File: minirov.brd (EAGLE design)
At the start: 65.8 x 30.7 mm, 55 parts, among them Q1 DMN6140L-13DICT-ND, Q2 DMN6140L-13DICT-ND, U1 DRV8848PWP, U2 DRV8848PWP, U3 MAX1136EUA-T

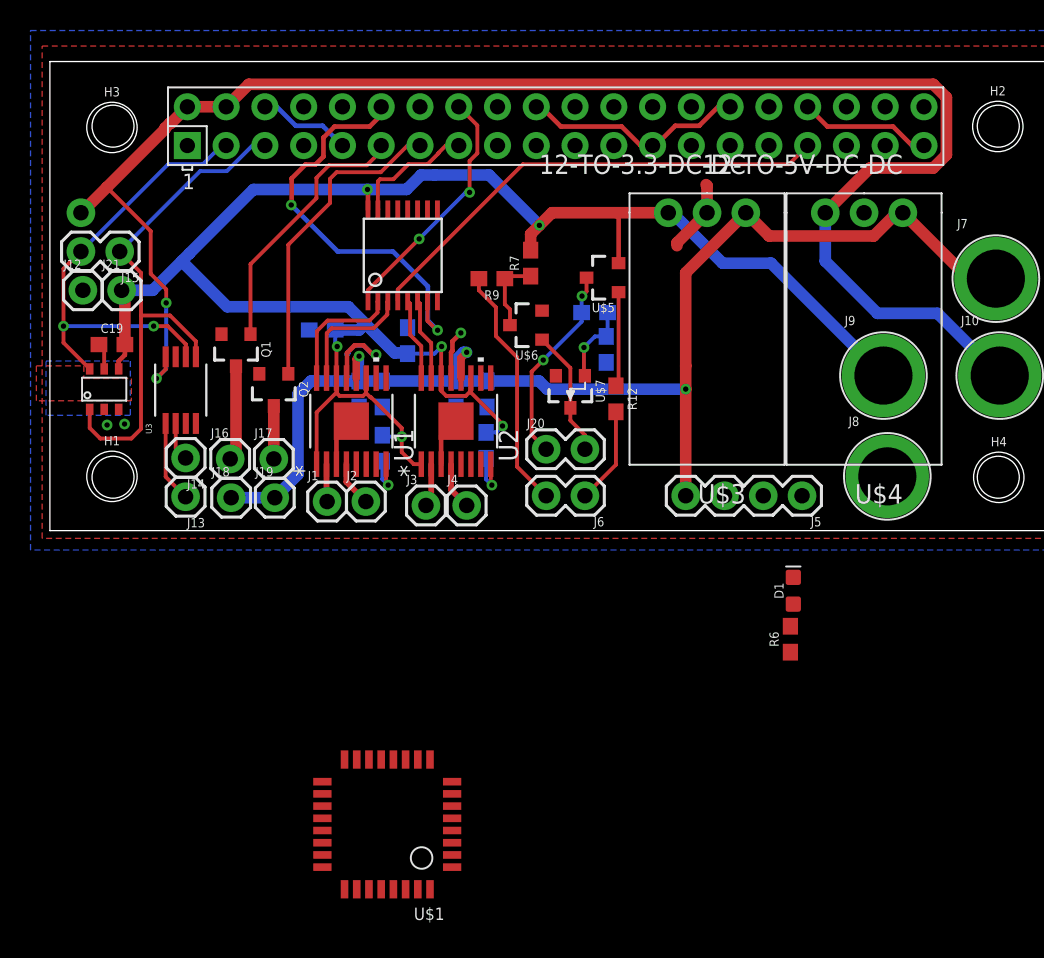
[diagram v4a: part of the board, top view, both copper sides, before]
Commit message: schematic changes and board changes to reflect it
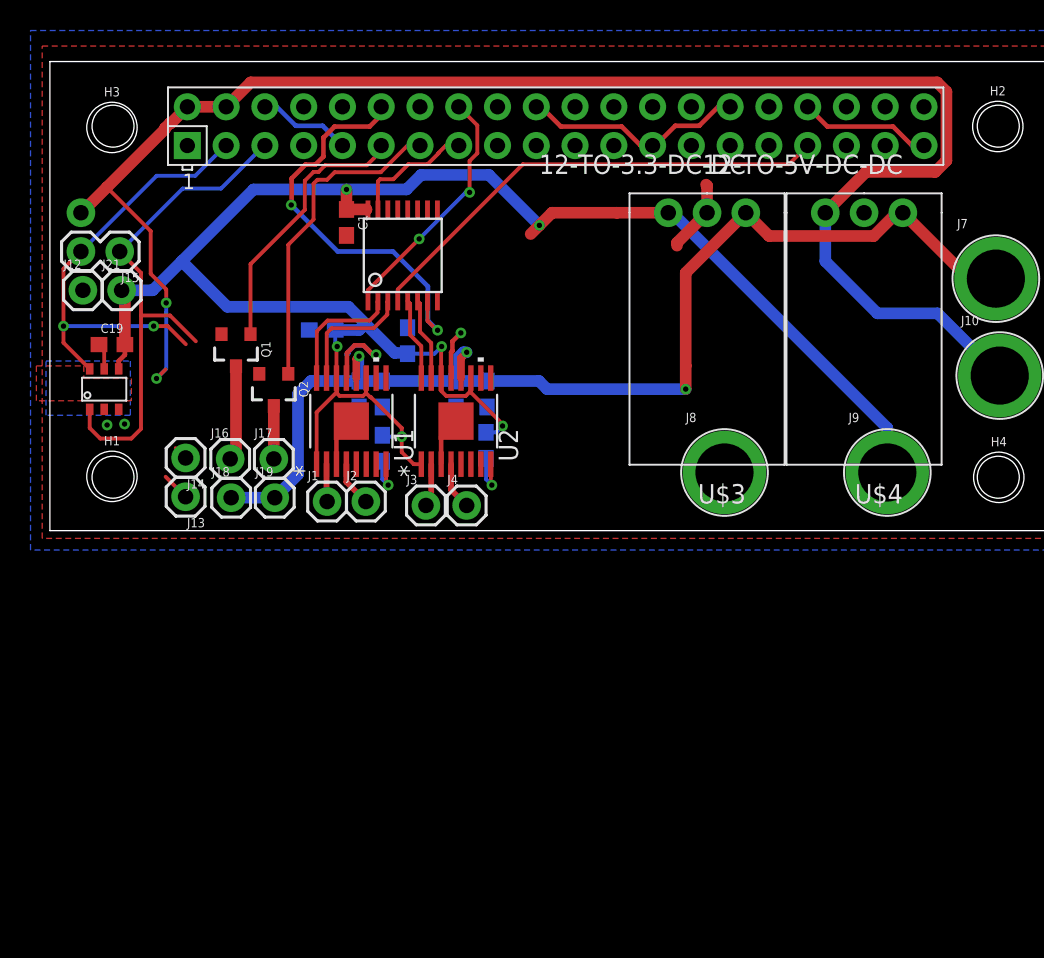
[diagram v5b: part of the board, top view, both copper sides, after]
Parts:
- removed C18: 10uF, SparkFun-Capacitors:0603
- removed D1: (no value), SparkFun-LED:LED-0603
- removed J20, J6: (no value), SparkFun-Connectors:1X02
- removed J5: (no value), SparkFun-Connectors:1X04
- removed R12, R9: 0, SparkFun-Resistors:0603
- removed R6: (no value), SparkFun-Resistors:0603
- removed R7, R8: 10k, SparkFun-Resistors:0603
- removed U$1: STM32F042K6T6, PI_Shield_Library:STM32F042K6T6
- removed U$5: UN2112, minirov:SOT23-3
- removed U$6: UN2212, minirov:SOT23-3
- removed U$7: BAS16, minirov:BAS16
- removed U3: MAX1136EUA-T, MAX1136EUA-T:21-0036K
- added C1: 100nF, SparkFun-Capacitors:0603
- moved J8 10.7 mm to (44.2, 3.81)
- moved J9 6.36 mm to (54.9, 3.81)
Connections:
- removed net CAN_H: J5.3
- removed net CAN_L: J5.2
- removed net CAN_STM_RX: U$1.PA11
- removed net CAN_STM_TX: U$1.PA12
- removed net HBEAT_LED: R6.1, U$1.PA15
- removed net N$1: U$9.8
- removed net N$2: U$9.10
- removed net N$4: D1.A, R6.2
- removed net N$5: C18.1, R8.1, U$7.1
- removed net OSC_IN: U$1.PF0-OSC_IN
- removed net OSC_OUT: U$1.PF1-OSC_OUT
- removed net RS-IN: J20.2, U$6.1, U$7.3
- removed net RS-OUT: J20.1, R8.2, U$5.3
- removed net RX: R12.1, U$5.1
- removed net SWCLK: U$1.PA14
- removed net SWDIO: U$1.PA13
- removed net TX: R7.1, R9.1, U$6.3
- removed net USART_RX: J6.1, R12.2, U$1.PA10
- removed net USART_TX: J6.2, R9.2, U$1.PA9
- net +12V: no longer J5.4
- net +3V3: now also C1.1; no longer R7.2, U$5.2
- net +5V: no longer U3.8
- net ADC_IN1: no longer U3.1
- net ADC_IN2: no longer U3.2
- net GND: now also C1.2; no longer C18.2, D1.C, J5.1, U$1.PB8-BOOT0, U$1.VSS, U$1.VSS1, U$6.2, U3.7
- net SCL: no longer U3.5
- net SDA: no longer U3.6
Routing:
- net USART_TX: track 16.0 -> 0.00 mm
- net RS-OUT: track 13.1 -> 0.00 mm, vias 2 -> 0
- net RS-IN: track 8.34 -> 0.00 mm
- net +12V: track 83.2 -> 76.2 mm
- net USART_RX: track 6.34 -> 0.00 mm
- net RX: track 6.21 -> 0.00 mm
- net N$5: track 5.24 -> 0.00 mm, vias 1 -> 0
- net TX: track 4.95 -> 0.00 mm
- net ADC_IN1: track 5.34 -> 1.85 mm
- net +3V3: track 123.7 -> 125.3 mm
- net ADC_IN2: track 2.53 -> 0.92 mm
- net SCL: track 35.0 -> 34.0 mm
- net SDA: track 30.6 -> 29.8 mm

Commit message: routing, deleting extraneous, and graphic
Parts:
- removed J13, J14: (no value), SparkFun-Connectors:1X01
- moved J8 4.06 mm to (48.3, 3.81)
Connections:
- removed net ADC_IN1: J13.1
- removed net ADC_IN2: J14.1
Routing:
- net +5V: track 107.4 -> 92.1 mm, vias 2 -> 0
- net SDA: track 29.8 -> 21.3 mm, vias 2 -> 0
- net +12V: track 76.2 -> 71.3 mm, vias 3 -> 2
- net SCL: track 34.0 -> 29.7 mm
- net ADC_IN1: track 1.85 -> 0.00 mm
- net +3V3: track 125.3 -> 123.5 mm, vias 6 -> 5
- net GND: track 52.4 -> 53.4 mm
- net ADC_IN2: track 0.92 -> 0.00 mm

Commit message: misc changes
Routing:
- net +12V: track 71.3 -> 70.4 mm
- net +3V3: track 123.5 -> 124.3 mm
- net GND: track 53.4 -> 53.2 mm, vias 4 -> 3
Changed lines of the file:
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@@
 <layer number="196" name="mValues" color="7" fill="1" visible="no" active="yes"/>
 <layer number="199" name="Contour" color="7" fill="1" visible="yes" active="yes"/>
-<layer number="200" name="200bmp" color="1" fill="10" visible="yes" active="yes"/>
+<layer number="200" name="200bmp" color="1" fill="10" visible="no" active="yes"/>
 <layer number="201" name="201bmp" color="2" fill="10" visible="yes" active="yes"/>
 <layer number="202" name="202bmp" color="3" fill="10" visible="yes" active="yes"/>
@@
 <vertex x="5.334" y="9.9695"/>
 <vertex x="5.334" y="8.509"/>
+<vertex x="1.9304" y="8.509"/>
+<vertex x="1.9304" y="6.4008"/>
+<vertex x="-0.889" y="6.4008"/>
 <vertex x="-0.889" y="8.509"/>
 </polygon>
@@
 <wire x1="25.631484375" y1="4.3561" x2="25.631484375" y2="6.200484375" width="0.3048" layer="1"/>
 <wire x1="25.631484375" y1="6.200484375" x2="26.6065" y2="7.1755" width="0.3048" layer="1"/>
-<via x="26.924" y="12.954" extent="1-16" drill="0.35"/>
-<wire x1="26.28149375" y1="9.9949" x2="26.28149375" y2="11.68018125" width="0.3048" layer="1"/>
-<wire x1="26.28149375" y1="11.68018125" x2="26.37288125" y2="11.77156875" width="0.3048" layer="1"/>
-<wire x1="26.37288125" y1="12.40288125" x2="26.924" y2="12.954" width="0.3048" layer="1"/>
-<wire x1="26.37288125" y1="11.77156875" x2="26.37288125" y2="12.40288125" width="0.3048" layer="1"/>
 <via x="21.371940625" y="11.529440625" extent="1-16" drill="0.35"/>
 <wire x1="19.42349375" y1="9.9949" x2="19.46390625" y2="10.0353125" width="0.3048" layer="1"/>
@@
 <wire x1="43.053" y1="20.828" x2="43.053" y2="22.7584" width="0.762" layer="16"/>
 <wire x1="43.053" y1="20.828" x2="40.259" y2="18.034" width="0.762" layer="16"/>
+<wire x1="26.28149375" y1="9.9949" x2="26.28149375" y2="7.50050625" width="0.254" layer="1"/>
+<wire x1="26.28149375" y1="7.50050625" x2="26.6065" y2="7.1755" width="0.254" layer="1"/>
 <wire x1="25.389" y1="15.034" x2="23.4315" y2="13.296" width="0" layer="19" extent="1-16"/>
 <wire x1="19.7485" y1="7.1755" x2="20.2565" y2="8.1035" width="0" layer="19" extent="1-16"/>
@@
 <wire x1="8.636" y1="17.653" x2="6.731" y2="15.748" width="0.762" layer="16"/>
 <wire x1="8.636" y1="17.653" x2="11.6205" y2="14.6685" width="0.762" layer="16"/>
-<wire x1="27.56650625" y1="9.146925" x2="27.24608125" y2="8.8265" width="0.254" layer="1"/>
-<wire x1="25.96691875" y1="8.8265" x2="25.64649375" y2="9.146925" width="0.254" layer="1"/>
 <wire x1="27.581515625" y1="9.9949" x2="27.56650625" y2="9.979890625" width="0.254" layer="1"/>
-<wire x1="27.56650625" y1="9.979890625" x2="27.56650625" y2="9.146925" width="0.254" layer="1"/>
-<wire x1="25.64649375" y1="9.146925" x2="25.64649375" y2="9.979890625" width="0.254" layer="1"/>
+<wire x1="27.56650625" y1="9.979890625" x2="27.56650625" y2="9.06746875" width="0.254" layer="1"/>
 <wire x1="25.64649375" y1="9.979890625" x2="25.631484375" y2="9.9949" width="0.254" layer="1"/>
-<wire x1="27.24608125" y1="8.8265" x2="25.96691875" y2="8.8265" width="0.254" layer="1"/>
 <wire x1="20.70850625" y1="9.019925" x2="20.51508125" y2="8.8265" width="0.254" layer="1"/>
 <wire x1="18.98191875" y1="8.8265" x2="18.78849375" y2="9.019925" width="0.254" layer="1"/>
@@
 <wire x1="29.2345" y1="6.438" x2="28.575" y2="6.438" width="0.254" layer="16"/>
 <wire x1="29.6545" y1="6.858" x2="29.2345" y2="6.438" width="0.254" layer="16"/>
-<wire x1="27.56650625" y1="9.06746875" x2="27.56650625" y2="9.146925" width="0.254" layer="1"/>
 <wire x1="29.6545" y1="6.979475" x2="27.56650625" y2="9.06746875" width="0.254" layer="1"/>
 <wire x1="24.331459375" y1="4.3561" x2="23.8379" y2="4.3561" width="0.254" layer="1"/>
@@
 <wire x1="40.513" y1="20.828" x2="54.864" y2="6.477" width="0.762" layer="1"/>
 <wire x1="54.864" y1="6.477" x2="54.864" y2="3.81" width="0.762" layer="1"/>
+<wire x1="25.73788125" y1="12.1384" x2="27.0545125" y2="12.1384" width="0.254" layer="1"/>
+<wire x1="27.0545125" y1="12.1384" x2="27.56650625" y2="11.62640625" width="0.254" layer="1"/>
+<wire x1="27.56650625" y1="11.62640625" x2="27.56650625" y2="9.979890625" width="0.254" layer="1"/>
+<wire x1="25.66448125" y1="12.065" x2="25.73788125" y2="12.1384" width="0.254" layer="1"/>
 <wire x1="20.7448" y1="21.034" x2="20.839" y2="21.034" width="0" layer="19" extent="1-1"/>
 </signal>
@@
 <wire x1="11.8745" y1="2.159" x2="14.732" y2="2.159" width="0.762" layer="16"/>
 <wire x1="26.946515625" y1="10.009909375" x2="26.93150625" y2="9.9949" width="0.254" layer="1"/>
-<via x="27.305" y="11.684" extent="1-16" drill="0.35"/>
+<via x="26.7716" y="11.4554" extent="1-16" drill="0.35"/>
 <wire x1="26.6065" y1="9.8035" x2="26.6065" y2="11.19751875" width="0.762" layer="16"/>
-<wire x1="26.6065" y1="11.19751875" x2="27.09298125" y2="11.684" width="0.762" layer="16"/>
-<wire x1="26.93150625" y1="9.9949" x2="26.93150625" y2="11.31050625" width="0.508" layer="1"/>
-<wire x1="26.93150625" y1="11.31050625" x2="27.305" y2="11.684" width="0.508" layer="1"/>
+<wire x1="26.6065" y1="11.19751875" x2="26.7716" y2="11.36261875" width="0.762" layer="16"/>
+<wire x1="26.93150625" y1="9.9949" x2="26.93150625" y2="11.29549375" width="0.508" layer="1"/>
+<wire x1="26.93150625" y1="11.29549375" x2="26.7716" y2="11.4554" width="0.508" layer="1"/>
 <wire x1="20.07350625" y1="9.9949" x2="20.07350625" y2="11.24700625" width="0.508" layer="1"/>
 <wire x1="20.07350625" y1="11.24700625" x2="20.2565" y2="11.43" width="0.508" layer="1"/>
 <via x="20.2565" y="11.43" extent="1-16" drill="0.35"/>
 <wire x1="20.2565" y1="11.43" x2="20.2565" y2="9.8035" width="0.6604" layer="16"/>
-<wire x1="27.09298125" y1="11.684" x2="27.305" y2="11.684" width="0.762" layer="16"/>
+<wire x1="26.7716" y1="11.4554" x2="26.7716" y2="11.36261875" width="0.762" layer="16"/>
 <wire x1="17.106" y1="9.8035" x2="16.256" y2="8.9535" width="0.762" layer="16"/>
 <wire x1="16.256" y1="8.9535" x2="16.256" y2="3.683" width="0.762" layer="16"/>
@@
 <contactref element="U$2" pad="2B1"/>
 <contactref element="U2" pad="16"/>
-<wire x1="23.439" y1="15.034" x2="23.5988" y2="14.8742" width="0.254" layer="1"/>
+<wire x1="23.439" y1="15.034" x2="23.4464" y2="15.0266" width="0.254" layer="1"/>
 <wire x1="24.331459375" y1="12.088628125" x2="24.331459375" y2="9.9949" width="0.254" layer="1"/>
-<wire x1="23.5988" y1="14.8742" x2="23.5988" y2="12.8212875" width="0.254" layer="1"/>
-<wire x1="23.5988" y1="12.8212875" x2="24.331459375" y2="12.088628125" width="0.254" layer="1"/>
+<wire x1="23.4464" y1="15.0266" x2="23.4464" y2="12.9736875" width="0.254" layer="1"/>
+<wire x1="23.4464" y1="12.9736875" x2="24.331459375" y2="12.088628125" width="0.254" layer="1"/>
 </signal>
 <signal name="MTR_2B_PWM">
 <contactref element="U$2" pad="2B2"/>
 <contactref element="U2" pad="15"/>
-<wire x1="24.089" y1="15.034" x2="24.2488" y2="14.8742" width="0.254" layer="1"/>
-<wire x1="24.2488" y1="14.8742" x2="24.2488" y2="13.027225" width="0.254" layer="1"/>
-<wire x1="24.2488" y1="13.027225" x2="24.981471875" y2="12.294553125" width="0.254" layer="1"/>
+<wire x1="24.089" y1="15.034" x2="24.0964" y2="15.0266" width="0.254" layer="1"/>
+<wire x1="24.0964" y1="15.0266" x2="24.0964" y2="13.179625" width="0.254" layer="1"/>
+<wire x1="24.0964" y1="13.179625" x2="24.981471875" y2="12.294553125" width="0.254" layer="1"/>
 <wire x1="24.981471875" y1="12.294553125" x2="24.981471875" y2="9.9949" width="0.254" layer="1"/>
 </signal>

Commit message: Changes i forgot to push
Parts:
- removed H1, H2, H3, H4: STAND-OFF, SparkFun-Hardware:STAND-OFF
- added C10, C2, C3, C4, C5, C9: 0.1uF, SparkFun-Capacitors:0603
- added C11: 0.01uF, SparkFun-Capacitors:0603
- added C6: 10uF, SparkFun-Capacitors:0603
- added C7, C8: 18pF, SparkFun-Capacitors:0603
- added D1, D3: (no value), SparkFun-LED:LED-0603
- added D2, D4, D5: BLUE, SparkFun-LED:LED-0603
- added FB1: (no value), SparkFun-Coils:0603
- added R1: 10k, SparkFun-Resistors:0603
- added R10, R11: 1k, SparkFun-Resistors:0603
- added R12, R13, R14: (no value), SparkFun-Resistors:0603
- added R2: 100k, SparkFun-Resistors:0603
- added R3: 2.2k 1%, SparkFun-Resistors:0603
- added R6, R7, R8, R9: 49.9 1%, SparkFun-Resistors:0603
- added U3: (no value), microbuilder:SSOP28DB
- added U4: S811-1X1T-06-F, mini_rov_magjack:S811-1X1T
- added Y1: ABM8-25.000MHZ-B2-T, ABM8-25.000MHZ-B2-T:OSCSC320X250X100N
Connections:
- new net CS: R2.1, U$9.24, U3.9
- new net INT: U$9.22, U3.4
- new net LEDA: R10.2, U3.27
- new net LEDB: R11.2, U3.26
- new net N$1: C7.2, U3.23, Y1.1
- new net N$12: U3.5
- new net N$14: U3.3
- new net N$2: C8.1, U3.24, Y1.3
- new net N$25: R3.1, U3.14
- new net N$26: C6.1, U3.1
- new net N$29: C10.2, FB1.2, R6.1, R7.1, U4.1
- new net N$3: D5.A, R12.1
- new net N$32: C11.1, R8.1, R9.1
- new net N$4: D1.A, R10.1
- new net N$5: D3.A, R11.1
- new net N$8: D2.A, R13.1
- new net N$9: D4.A, R14.1
- new net RST: R1.1, U3.10
- new net TPIN+: R8.2, U3.13, U4.4
- new net TPIN-: R9.2, U3.12, U4.5
- new net TPOUT+: R6.2, U3.17, U4.2
- new net TPOUT-: R7.2, U3.16, U4.3
- net +12V: now also R14.2
- net +3V3: now also C2.1, C3.1, C4.1, C5.1, C9.2, FB1.1, R1.2, R12.2, R2.2, U3.15, U3.19, U3.20, U3.25, U3.28
- net +5V: now also R13.2
- net GND: now also C10.1, C11.2, C2.2, C3.2, C4.2, C5.2, C6.2, C7.1, C8.2, C9.1, D1.C, D2.C, D3.C, D4.C, D5.C, R3.2, U3.11, U3.18, U3.2, U3.21, U3.22, Y1.2, Y1.4
- net MISO: now also U3.6
- net MOSI: now also U3.7
- net SCK: now also U3.8
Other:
- board size 65.8 x 30.7 mm -> 65.8 x 51.6 mm
